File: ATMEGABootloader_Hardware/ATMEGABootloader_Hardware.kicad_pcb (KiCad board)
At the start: 2 copper layers, 55.9 x 52.8 mm, 9 parts, among them U1 ATmega328-PU, Y1 16MHz

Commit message: did silkscreen
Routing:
- net Rx: track 0.00 -> 77.2 mm
- net Tx: track 0.00 -> 63.8 mm
- net Rst: track 13.5 -> 52.7 mm
- net +5V: track 5.08 -> 33.2 mm
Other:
- board text added: "ATMEGA Flashing Board, Rev 1 Mars Rover Design Team Missouri S&T, 2019 Andrew Van Horn"
- board text added: "Reset Pullup"
- board text added: "Rx Disable"
- board text added: "XTAL Enable"
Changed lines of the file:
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@@
   (general
     (thickness 1.6)
-    (drawings 8)
-    (tracks 37)
+    (drawings 12)
+    (tracks 62)
     (zones 0)
     (modules 9)
@@
     )
   )
+  (gr_text "ATMEGA Flashing Board, Rev 1\nMars Rover Design Team\nMissouri S&T, 2019\nAndrew Van Horn" (at 141.986 78.232) (layer F.SilkS)
+    (effects (font (size 1.5 1.5) (thickness 0.3)) (justify left))
+  )
+  (gr_text "Reset\nPullup" (at 168.402 87.63 270) (layer F.SilkS)
+    (effects (font (size 1.5 1.5) (thickness 0.3)))
+  )
+  (gr_text "Rx\nDisable" (at 150.622 107.95 270) (layer F.SilkS)
+    (effects (font (size 1.5 1.5) (thickness 0.3)))
+  )
+  (gr_text "XTAL\nEnable" (at 168.148 107.95 270) (layer F.SilkS)
+    (effects (font (size 1.5 1.5) (thickness 0.3)))
+  )
   (gr_line (start 140.716 71.628) (end 140.716 119.38) (layer Edge.Cuts) (width 0.15))
   (gr_line (start 196.596 119.38) (end 196.596 71.628) (layer Edge.Cuts) (width 0.15))
@@
   (gr_arc (start 143.256 71.628) (end 143.256 69.088) (angle -90) (layer Edge.Cuts) (width 0.15))
   (segment (start 172.72 93.98) (end 172.72 88.9) (width 0.381) (layer F.Cu) (net 11))
+  (segment (start 172.72 96.52) (end 167.64 101.6) (width 0.381) (layer F.Cu) (net 11))
+  (segment (start 172.72 93.98) (end 172.72 96.52) (width 0.381) (layer F.Cu) (net 11))
+  (segment (start 169.16 103.12) (end 167.64 101.6) (width 0.381) (layer F.Cu) (net 11))
+  (segment (start 169.16 119.38) (end 169.16 103.12) (width 0.381) (layer F.Cu) (net 11))
   (segment (start 167.64 71.12) (end 167.64 79.502) (width 0.381) (layer F.Cu) (net 19))
   (segment (start 167.64 79.502) (end 167.668 79.53) (width 0.381) (layer F.Cu) (net 19))
@@
   (segment (start 172.72 79.53) (end 172.145 79.53) (width 0.381) (layer F.Cu) (net 19))
   (segment (start 172.117 79.502) (end 167.64 79.502) (width 0.381) (layer F.Cu) (net 19))
+  (segment (start 153.162 79.502) (end 167.64 79.502) (width 0.381) (layer F.Cu) (net 19))
+  (segment (start 151.384 79.502) (end 153.162 79.502) (width 0.381) (layer F.Cu) (net 19))
+  (segment (start 150.876 80.01) (end 151.384 79.502) (width 0.381) (layer F.Cu) (net 19))
+  (segment (start 150.876 98.895) (end 150.876 80.01) (width 0.381) (layer F.Cu) (net 19))
+  (segment (start 152.4 100.419) (end 150.876 98.895) (width 0.381) (layer F.Cu) (net 19))
+  (segment (start 152.4 101.6) (end 152.4 100.419) (width 0.381) (layer F.Cu) (net 19))
   (segment (start 165.1 72.644) (end 165.1 71.12) (width 0.381) (layer B.Cu) (net 21))
   (segment (start 165.608 73.152) (end 165.1 72.644) (width 0.381) (layer B.Cu) (net 21))
-  (segment (start 179.578 73.152) (end 165.608 73.152) (width 0.381) (layer B.Cu) (net 21))
-  (segment (start 180.34 93.98) (end 180.34 73.914) (width 0.381) (layer B.Cu) (net 21))
-  (segment (start 180.34 73.914) (end 179.578 73.152) (width 0.381) (layer B.Cu) (net 21))
+  (segment (start 179.832 73.152) (end 165.608 73.152) (width 0.381) (layer B.Cu) (net 21))
+  (segment (start 180.34 93.98) (end 180.34 73.66) (width 0.381) (layer B.Cu) (net 21))
+  (segment (start 180.34 73.66) (end 179.832 73.152) (width 0.381) (layer B.Cu) (net 21))
   (segment (start 162.56 73.406) (end 162.56 71.12) (width 0.381) (layer B.Cu) (net 23))
   (segment (start 163.068 73.914) (end 162.56 73.406) (width 0.381) (layer B.Cu) (net 23))
@@
   (segment (start 175.26 93.98) (end 175.26 75.184) (width 0.381) (layer B.Cu) (net 25))
   (segment (start 175.26 75.184) (end 174.752 74.676) (width 0.381) (layer B.Cu) (net 25))
+  (segment (start 158.75 108.712) (end 158.242 109.22) (width 0.381) (layer B.Cu) (net 29))
+  (segment (start 158.75 98.298) (end 158.75 108.712) (width 0.381) (layer B.Cu) (net 29))
+  (segment (start 158.242 109.22) (end 154.94 109.22) (width 0.381) (layer B.Cu) (net 29))
+  (segment (start 194.56 72.25137) (end 194.818 72.50937) (width 0.381) (layer B.Cu) (net 29))
+  (segment (start 194.56 71.12) (end 194.56 72.25137) (width 0.381) (layer B.Cu) (net 29))
+  (segment (start 194.818 72.50937) (end 194.818 97.282) (width 0.381) (layer B.Cu) (net 29))
+  (segment (start 194.818 97.282) (end 194.31 97.79) (width 0.381) (layer B.Cu) (net 29))
+  (segment (start 194.31 97.79) (end 159.258 97.79) (width 0.381) (layer B.Cu) (net 29))
+  (segment (start 159.258 97.79) (end 158.75 98.298) (width 0.381) (layer B.Cu) (net 29))
+  (segment (start 157.48 98.552) (end 157.48 101.6) (width 0.381) (layer B.Cu) (net 30))
+  (segment (start 159.004 97.028) (end 157.48 98.552) (width 0.381) (layer B.Cu) (net 30))
+  (segment (start 191.516 97.028) (end 159.004 97.028) (width 0.381) (layer B.Cu) (net 30))
+  (segment (start 192.024 96.52) (end 191.516 97.028) (width 0.381) (layer B.Cu) (net 30))
+  (segment (start 192.02 96.516) (end 192.024 96.52) (width 0.381) (layer B.Cu) (net 30))
+  (segment (start 192.02 71.12) (end 192.02 96.516) (width 0.381) (layer B.Cu) (net 30))
   (segment (start 180.54 114.1) (end 180.34 114.3) (width 0.381) (layer F.Cu) (net 31))
   (segment (start 180.54 109.22) (end 180.54 114.1) (width 0.381) (layer F.Cu) (net 31))

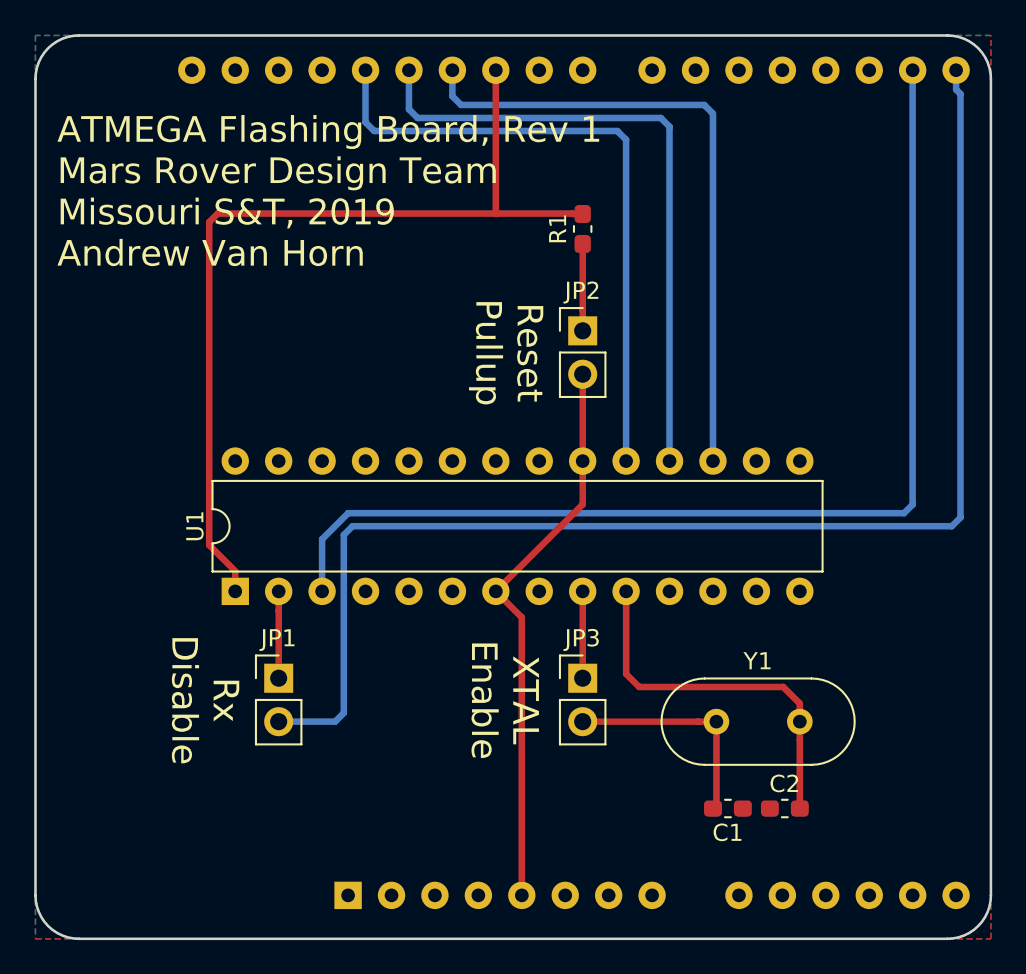
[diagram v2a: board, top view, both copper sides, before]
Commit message: Fixed RST routing and re generated gerbs
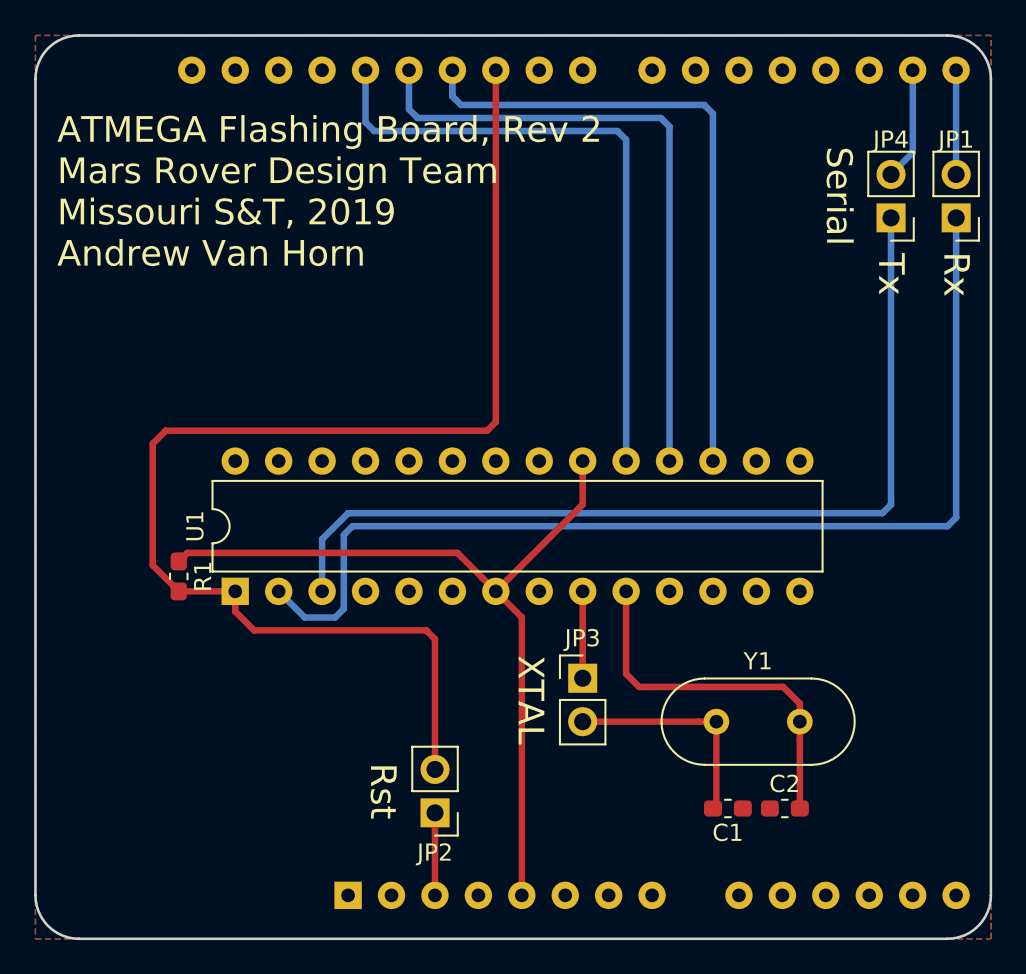
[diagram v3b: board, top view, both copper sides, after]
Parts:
- added JP4: Jumper, Connector_PinHeader_2.54mm:PinHeader_1x02_P2.54mm_Vertical, F.Cu at (190.8, 79.8)
- moved JP1 47.9 mm to (194.6, 79.8), turned to 180 degrees
- moved R1 31.2 mm to (149.1, 100.7), turned to 270 degrees
- moved JP2 29.5 mm to (164.1, 114.6), turned to 180 degrees
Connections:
- net P17 renamed D11
- net P18 renamed D12
- net P19 renamed D13
- JP2 pad 1: Net-(JP2-Pad1) -> Net-(A1-Pad3)
- JP2 pad 2: +5V -> Rst
- R1 pad 1: Net-(JP2-Pad1) -> +5V
- U1 pad 3: Tx -> Net-(JP4-Pad1)
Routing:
- net Rx: track 77.2 -> 6.10 mm
- net Net-(JP1-Pad1): track 5.08 -> 62.7 mm
- net Tx: track 63.8 -> 6.62 mm
- net Net-(JP4-Pad1): track 0.00 -> 53.9 mm
- net Rst: track 52.7 -> 74.9 mm
- net +5V: track 33.2 -> 47.8 mm
- net Net-(JP2-Pad1): track 5.08 -> 0.00 mm
- net Net-(A1-Pad3): track 0.00 -> 4.83 mm
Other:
- board text added: "ATMEGA Flashing Board, Rev 2 Mars Rover Design Team Missouri S&T, 2019 Andrew Van Horn"
- board text added: "Rst"
- board text added: "Rx"
- board text added: "Serial"
- board text added: "Tx"
- board text added: "XTAL"
- board text removed: "ATMEGA Flashing Board, Rev 1 Mars Rover Design Team Missouri S&T, 2019 Andrew Van Horn"
- board text removed: "Reset Pullup"
- board text removed: "Rx Disable"
- board text removed: "XTAL Enable"

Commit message: rerouted reset track
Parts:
- added G***: LOGO, MRDT_Silkscreens:z_sig_Andrew_Van_Horn_Sig_15mm, F.Cu at (149.4, 84.6)
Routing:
- net GND: vias 0 -> 1
